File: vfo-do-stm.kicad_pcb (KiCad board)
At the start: 2 copper layers, 37 parts, among them J1 SWIM, J2 DC_in, J3 LO, J4 VFO, SW1 SW_FreqMinus, SW2 SW_FreqPlus, SW3 SW_Band, SW4 SW_Res, SW5 SW_NRST, U1 L7805, U2 LP3982IMM-3.3, U3 STM8S208C8, U4 LP3982IMM-3.3, U5 LP3982IMM-3.3, U6 Si5351A-B-GT

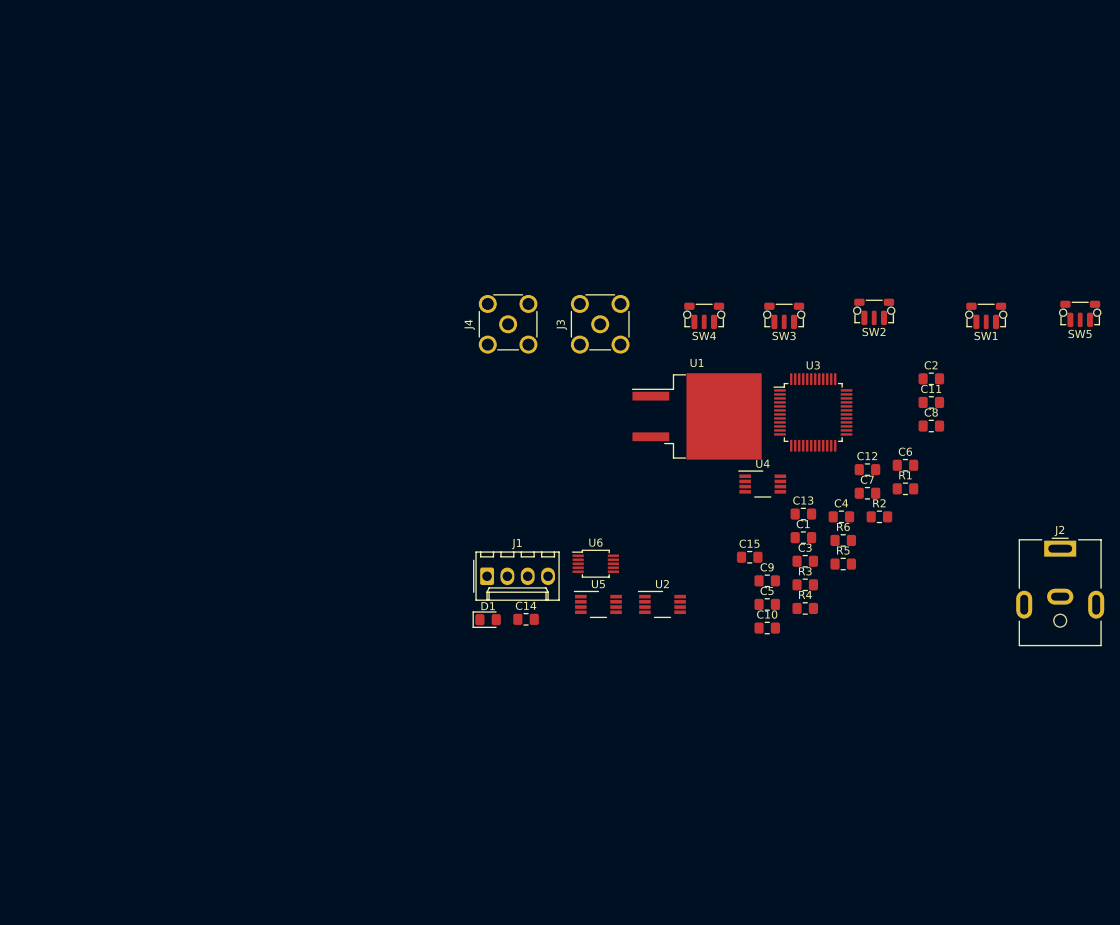
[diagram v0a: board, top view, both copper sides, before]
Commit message: Améliorations ébauche PCB
Ajout contour
Changement d'empreinte pour D1, J3, J4
Certains filtrages, découplages, résistance pullup/polldown sont encore manquants.
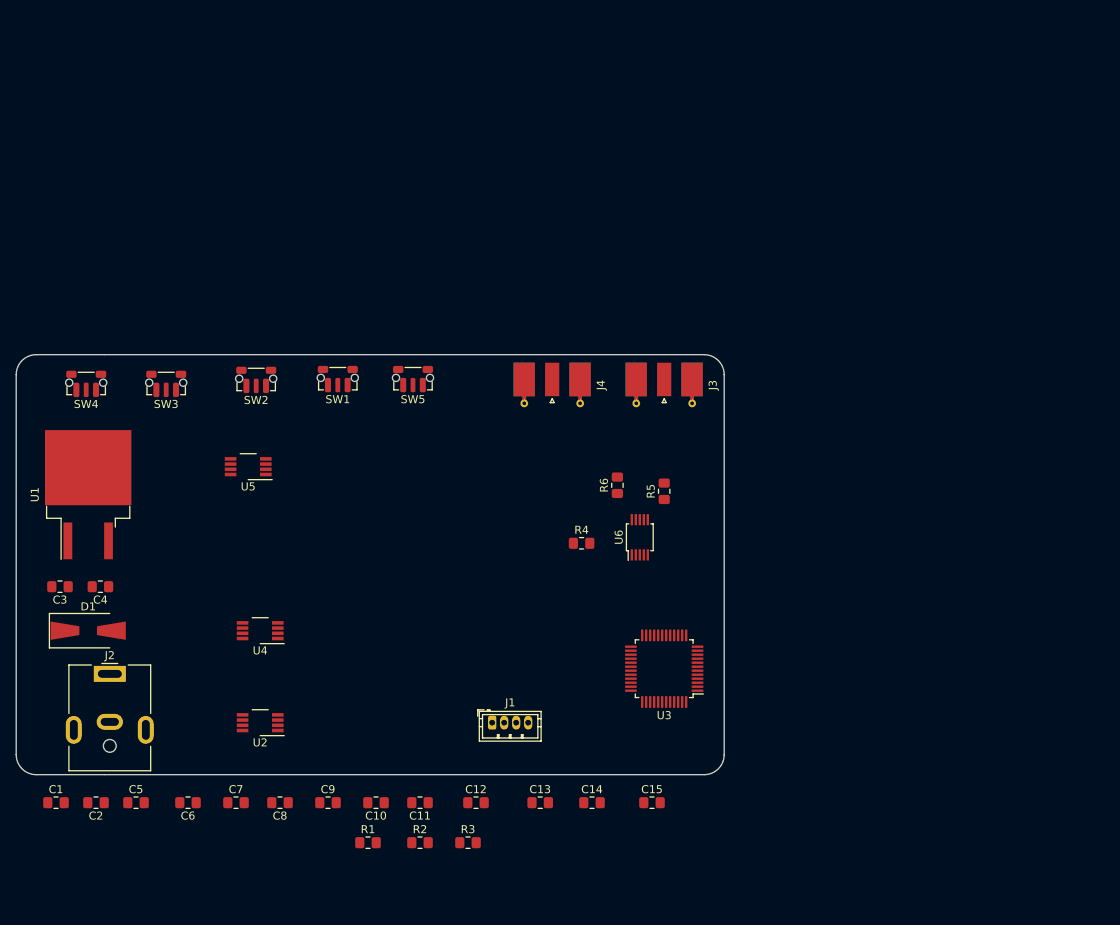
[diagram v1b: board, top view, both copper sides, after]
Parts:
- D1: footprint Diode_SMD:D_0805_2012Metric_Pad1.15x1.40mm_HandSolder -> Diode_SMD:D_SMA-SMB_Universal_Handsoldering
- J1: footprint Connector_Molex:Molex_KK-254_AE-6410-04A_1x04_P2.54mm_Vertical -> Connector_JST:JST_ZH_B4B-ZR_1x04_P1.50mm_Vertical
- J3, J4: footprint Connector_Coaxial:SMA_Molex_73251-2200_Horizontal -> Connector_Coaxial:SMA_Molex_73251-2120_EdgeMount_Horizontal
- moved J2 119.8 mm to (65.7, 119.9)
- moved C2 117.1 mm to (64.0, 136.0), turned to 180 degrees
- moved C1 99.1 mm to (59.0, 136.0)
- moved C6 99.1 mm to (75.5, 136.0), turned to 180 degrees
- moved C8 94.0 mm to (87.0, 136.0), turned to 180 degrees
- moved C3 93.2 mm to (59.5, 109.0), turned to 180 degrees
- moved C4 93.0 mm to (64.5, 109.0), turned to 180 degrees
- moved C7 87.9 mm to (81.5, 136.0)
- moved SW5 83.8 mm to (103.6, 82.9)
- moved C5 82.7 mm to (69.0, 136.0)
- moved SW1 81.4 mm to (94.2, 82.9)
- moved C11 81.2 mm to (104.5, 136.0), turned to 180 degrees
- moved R1 80.4 mm to (98.0, 141.0)
- moved SW2 77.7 mm to (84.0, 83.0)
- moved SW3 77.7 mm to (72.8, 83.5)
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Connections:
- net Net-(C1-Pad1) renamed /Net_5.5V
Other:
- board outline added: 88.5 x 52.5 mm
- net class CLK added: clearance 0.5, trace_width 1.5, via_dia 0.8, via_drill 0.4

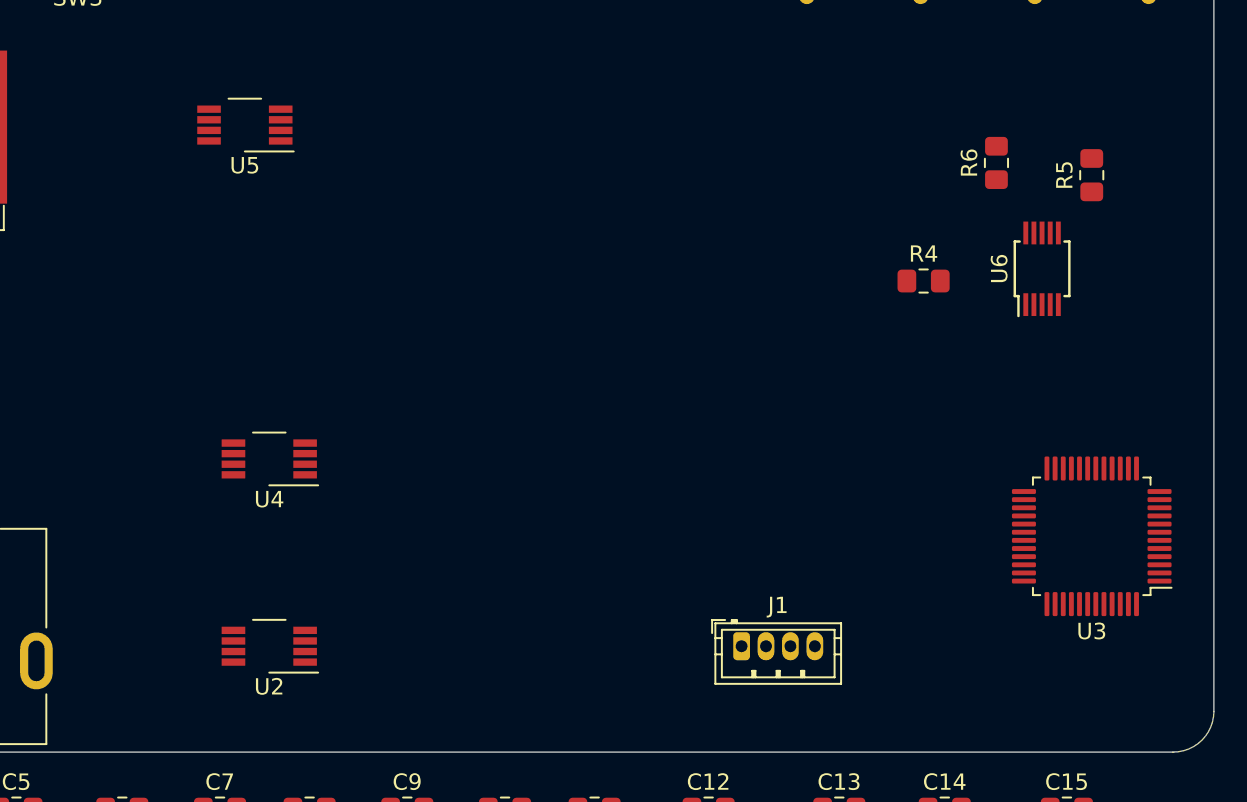
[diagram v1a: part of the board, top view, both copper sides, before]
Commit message: Update vfo-do-stm.kicad_pcb
Essai de placement MCU et réguls 3.3V
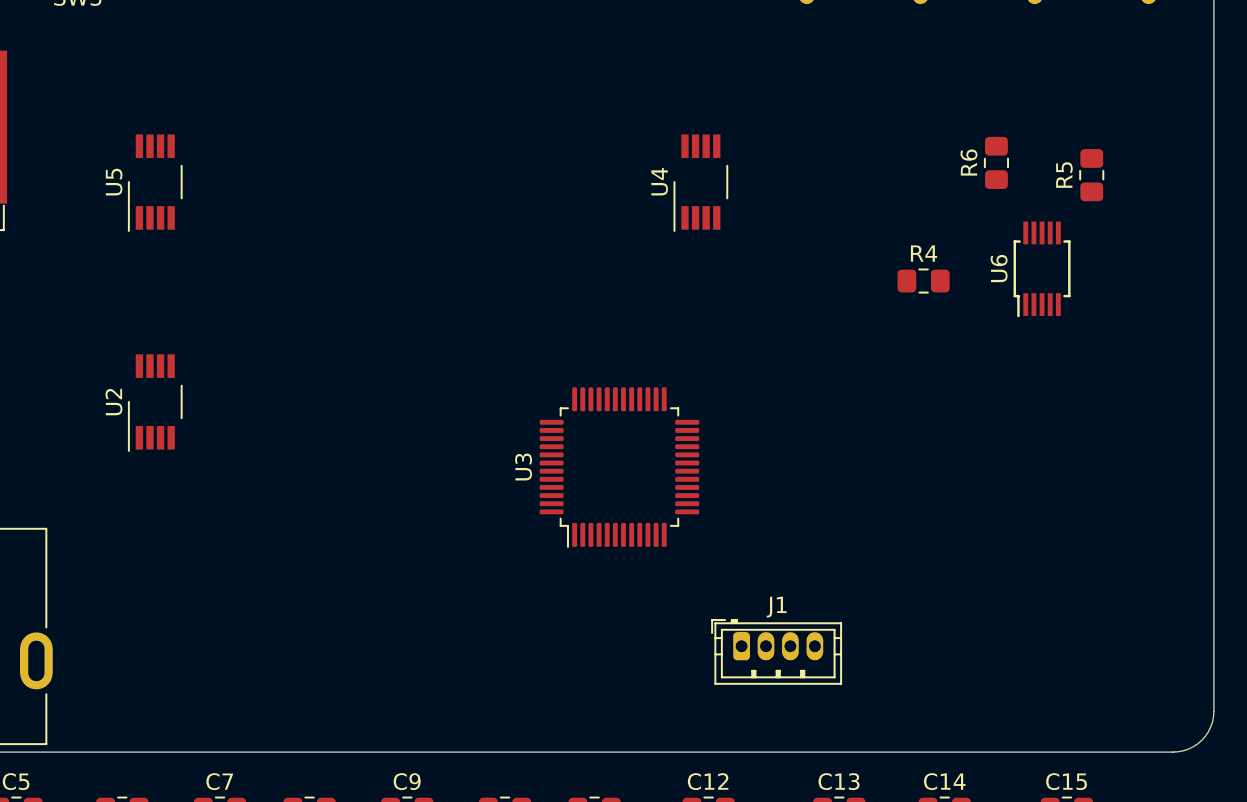
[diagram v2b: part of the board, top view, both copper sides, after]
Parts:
- moved U4 31.5 mm to (111.0, 97.5), turned to 90 degrees
- moved U3 29.3 mm to (106.0, 115.0), turned to 90 degrees
- moved U2 16.6 mm to (77.5, 111.0), turned to 90 degrees
- moved U5 6.52 mm to (77.5, 97.5), turned to 90 degrees

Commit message: Ebauche ecran
Ajout connecteur pour afficheur oled https://www.buydisplay.com/yellow-2-4-inch-graphic-oled-display-128x64-serial-spi-i2c-ssd1309
Renommage nets GPS -> CLK
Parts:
- added J5: Display, Connector_FFC-FPC:Molex_52435-2433_1x24-1MP_P0.5mm_Horizontal_TopContact, F.Cu at (80.0, 41.5)
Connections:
- net SHTDWN_GPS renamed SHTDWN_CLK
- C12 pad 1: 3.3GPS -> 3.3CLK
- C14 pad 1: 3.3MCU -> 3.3CLK
- C15 pad 1: 3.3MCU -> 3.3CLK
- R3 pad 1: 3.3GPS -> 3.3CLK
- U5 pad 1: 3.3GPS -> 3.3CLK
- U5 pad 4: 3.3GPS -> 3.3CLK
- U6 pad 1: 3.3MCU -> 3.3CLK
- U6 pad 7: 3.3MCU -> 3.3CLK

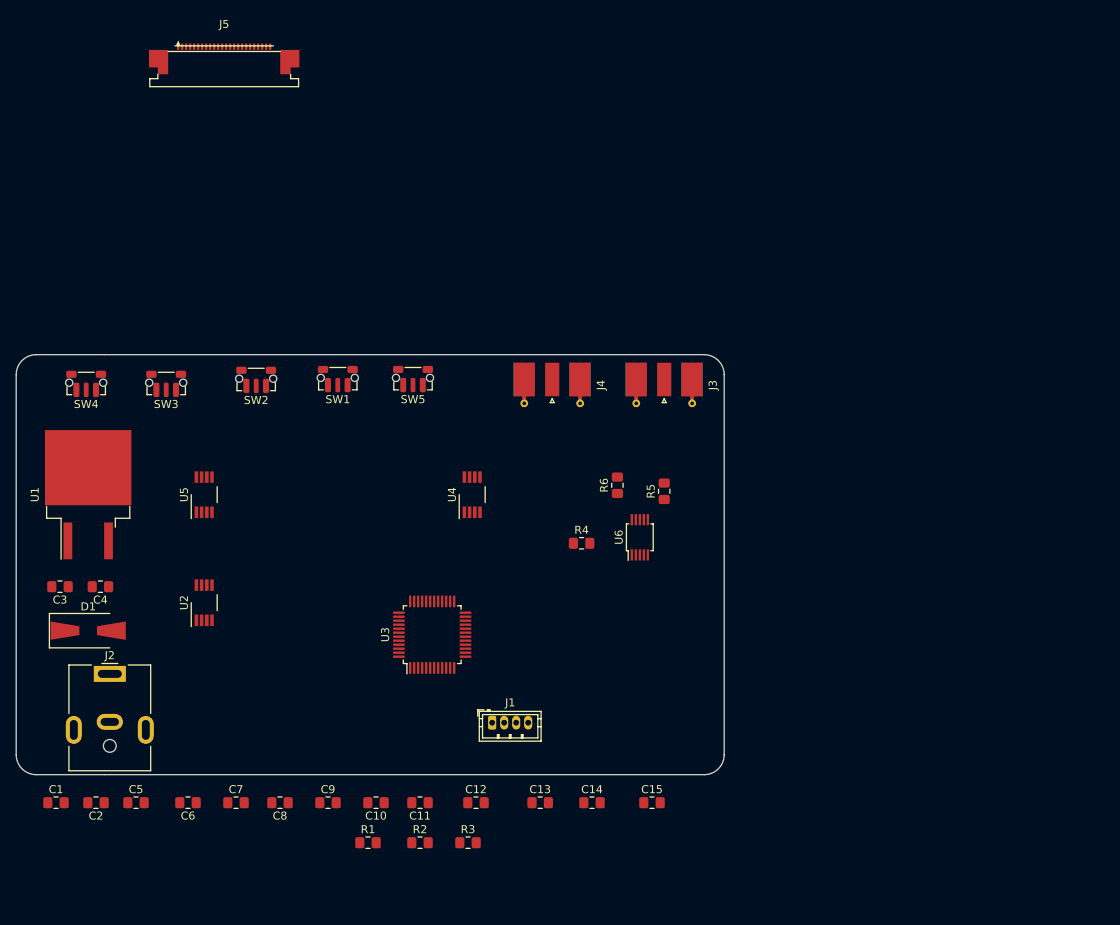
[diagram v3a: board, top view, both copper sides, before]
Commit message: Changement régul 3.3V & ajout expander I²C
Refonte de l'étage d'alim
Ajout d'une extension de 16 I/O en I²C
Retrait du connecteur écran
Ajout d'un crystal 24MHz pour le MCU
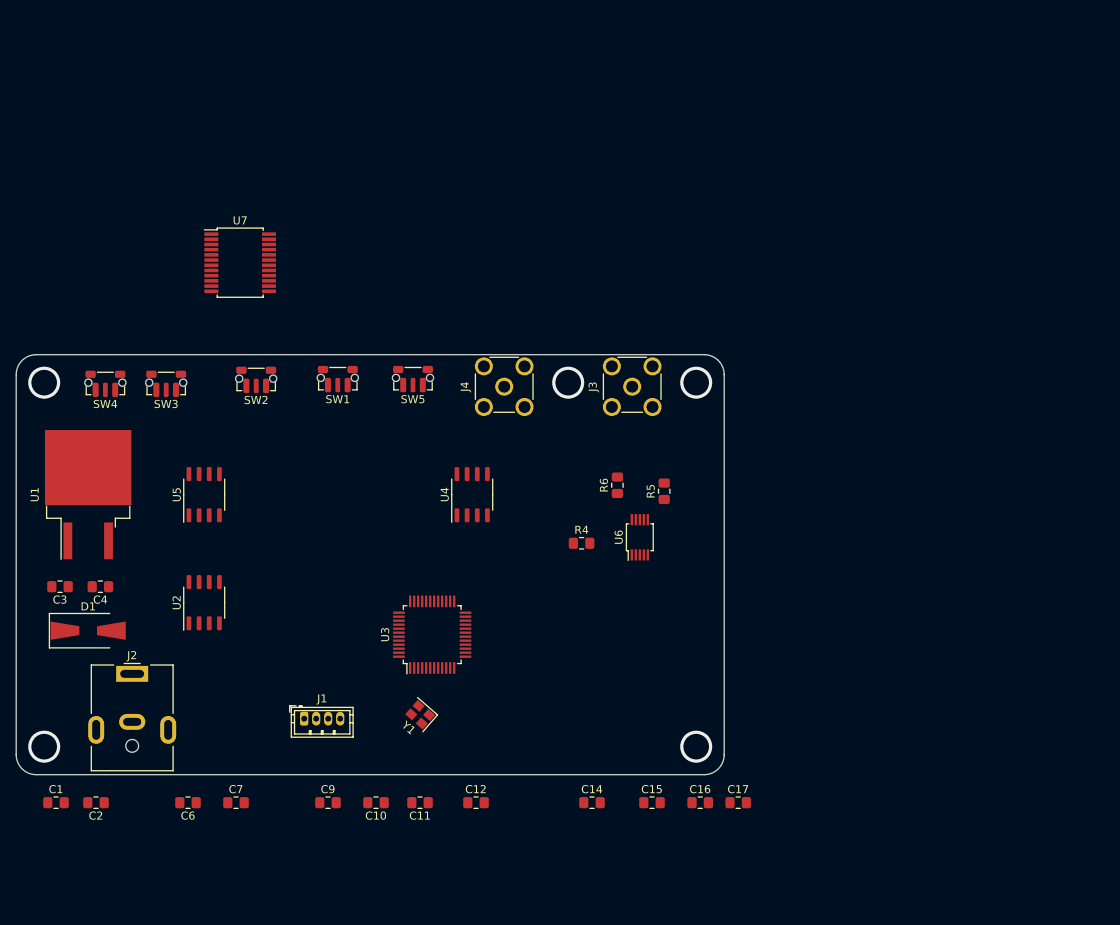
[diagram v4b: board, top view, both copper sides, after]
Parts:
- removed C13, C5, C8: 33nF, Capacitor_SMD:C_0805_2012Metric_Pad1.15x1.40mm_HandSolder
- removed J5: Display, Connector_FFC-FPC:Molex_52435-2433_1x24-1MP_P0.5mm_Horizontal_TopContact
- removed R1, R2, R3: 100kΩ, Resistor_SMD:R_0805_2012Metric_Pad1.15x1.40mm_HandSolder
- added C16: 20pF, Capacitor_SMD:C_0805_2012Metric_Pad1.15x1.40mm_HandSolder, F.Cu at (139.5, 136.0)
- added C17: 20pF, Capacitor_SMD:C_0805_2012Metric_Pad1.15x1.40mm_HandSolder, F.Cu at (144.2, 136.0)
- added U7: TCA9535DBR, Package_SO:SSOP-24_5.3x8.2mm_P0.65mm, F.Cu at (82.0, 68.5)
- added Y1: 24MHz, Crystal:Crystal_SMD_2520-4Pin_2.5x2.0mm, F.Cu at (104.5, 125.0)
- C1, C11, C6: value 2.2µF -> 0.1µF
- C12, C2, C7: value 2.2µF -> 10µF
- J3, J4: footprint Connector_Coaxial:SMA_Molex_73251-2120_EdgeMount_Horizontal -> Connector_Coaxial:SMA_Molex_73251-2200_Horizontal
- U2, U4, U5: value LP3982IMM-3.3 -> LE33CD; footprint Package_SO:VSSOP-8_3.0x3.0mm_P0.65mm -> Package_SO:SO-8_3.9x4.9mm_P1.27mm
- moved J1 23.5 mm to (90.0, 125.5)
- moved J4 6.07 mm to (115.0, 84.0), turned to 0 degrees
- moved J3 4.10 mm to (131.0, 84.0), turned to 0 degrees
- moved J2 2.80 mm to (68.5, 119.9)
- moved SW4 2.40 mm to (65.2, 83.5)
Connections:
- SW1 pad 1: GND -> Net-(SW1-Pad1)
- SW2 pad 1: GND -> Net-(SW2-Pad1)
- SW3 pad 1: GND -> Net-(SW3-Pad1)
- SW4 pad 1: GND -> Net-(SW4-Pad1)
- SW5 pad 1: GND -> Net-(SW5-Pad1)
- U2 pad 2: /Net_5.5V -> GND
- U2 pad 4: 3.3MCU -> Net-(U2-Pad4)
- U2 pad 5: Net-(U2-Pad5) -> GND
- U2 pad 6: Net-(C5-Pad1) -> GND
- U2 pad 7: /Net_5.5V -> GND
- U2 pad 8: Net-(R1-Pad2) -> /Net_5.5V
- U3 pad 26: Net-(SW1-Pad2) -> Net-(U3-Pad26)
- U3 pad 27: Net-(SW2-Pad2) -> Net-(U3-Pad27)
- U3 pad 28: Net-(SW3-Pad2) -> Net-(U3-Pad28)
- U3 pad 29: Net-(SW4-Pad2) -> Net-(U3-Pad29)
- U3 pad 39: SHTDWN_CLK -> INH_CLK
- U3 pad 40: SHTDWN_LCD -> INH_LCD
- U4 pad 2: /Net_5.5V -> GND
- U4 pad 4: 3.3LCD -> Net-(U4-Pad4)
- U4 pad 5: Net-(U4-Pad5) -> INH_LCD
- U4 pad 6: Net-(C8-Pad1) -> GND
- U4 pad 7: SHTDWN_LCD -> GND
- U4 pad 8: Net-(R2-Pad2) -> /Net_5.5V
- U5 pad 2: /Net_5.5V -> GND
- U5 pad 4: 3.3CLK -> Net-(U5-Pad4)
- U5 pad 5: Net-(U5-Pad5) -> INH_CLK
- U5 pad 6: Net-(C13-Pad1) -> GND
- U5 pad 7: SHTDWN_CLK -> GND
- U5 pad 8: Net-(R3-Pad2) -> /Net_5.5V
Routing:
- net GND: vias 0 -> 5
